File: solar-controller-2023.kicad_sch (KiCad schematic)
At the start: 0 parts

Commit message: add copyright notices
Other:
- note added: "Copyright (C) 2023"
- note added: "Jonathan Bagg"
- note added: "SOLAR CONTROLLER 2023"
- note added: "See https://creativecommons.org/licenses/by-nc-sa/4.0/"
- note added: "v1"

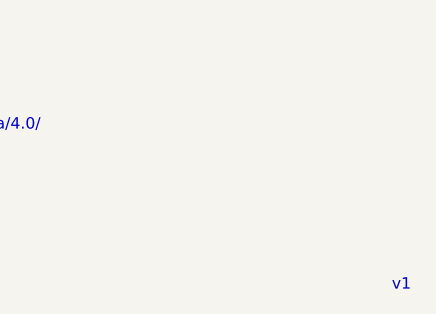
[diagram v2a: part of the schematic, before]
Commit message: AC couple LMT01 signal conditioning and add gain
The difference circuit U3A was DC coupled and so could not
have gain.  Unit gain was only good for sensors up to 15m of
cat-5.
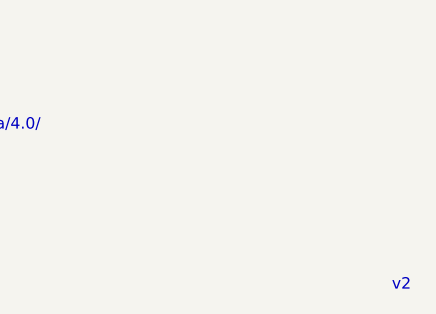
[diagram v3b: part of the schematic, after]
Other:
- note added: "v2"
- note removed: "v1"
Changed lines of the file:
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@@
     )
   )
-  (text "v1" (at 269.24 194.31 0)
+  (text "v2" (at 269.24 194.31 0)
     (effects (font (size 1.27 1.27)) (justify left bottom))
   )
@@
       (reference "#PWR018") (unit 1) (value "GND") (footprint "")
     )
-    (path "/493e9052-9256-45d2-b217-1231bb5dbb20/67602620-6a50-4ac8-bf48-765ca6ca3713"
-      (reference "#PWR019") (unit 1) (value "GND") (footprint "")
-    )
     (path "/493e9052-9256-45d2-b217-1231bb5dbb20/585baf59-dc3a-4d28-882c-d5894ff76c9c"
       (reference "#PWR020") (unit 1) (value "+3V3") (footprint "")
@@
     )
     (path "/493e9052-9256-45d2-b217-1231bb5dbb20/d3ec0c86-c83a-41fb-ba8d-d0db438240cb"
-      (reference "C20") (unit 1) (value "100nF") (footprint "Capacitor_SMD:C_0603_1608Metric_Pad1.08x0.95mm_HandSolder")
+      (reference "C20") (unit 1) (value "680pF") (footprint "Capacitor_SMD:C_0603_1608Metric_Pad1.08x0.95mm_HandSolder")
     )
     (path "/f0385cfa-6958-422f-a694-373ebd16af7a/e37d8436-904b-488c-a95d-9b93d5cb27a7"
@@
       (reference "C38") (unit 1) (value "100nF") (footprint "Capacitor_SMD:C_0603_1608Metric_Pad1.08x0.95mm_HandSolder")
     )
+    (path "/493e9052-9256-45d2-b217-1231bb5dbb20/323ed20a-1d8e-4e2b-96ae-40f84ff376ca"
+      (reference "C39") (unit 1) (value "680pF") (footprint "Capacitor_SMD:C_0603_1608Metric_Pad1.08x0.95mm_HandSolder")
+    )
     (path "/1de4833b-6322-4b99-b5c8-ec67a2e43a06/e530f387-2ae9-42c8-bfd3-533602f3058a"
       (reference "D1") (unit 1) (value "LED") (footprint "Diode_SMD:D_0603_1608Metric_Pad1.05x0.95mm_HandSolder")
@@
       (reference "OUT_7") (unit 1) (value "282837-2") (footprint "project_footprints:282837-2_TYC")
     )
-    (path "/493e9052-9256-45d2-b217-1231bb5dbb20/06b8b026-7bf7-4a1a-a49e-019d3279346a"
-      (reference "Q1") (unit 1) (value "MMBT3906") (footprint "Package_TO_SOT_SMD:SOT-23")
-    )
     (path "/1de4833b-6322-4b99-b5c8-ec67a2e43a06/fd382fec-b21c-4e2d-9067-fa342e870f53"
       (reference "Q2") (unit 1) (value "DTC113Z") (footprint "Package_TO_SOT_SMD:SOT-23")
@@
     )
     (path "/493e9052-9256-45d2-b217-1231bb5dbb20/739a4b9d-9201-4e8c-9e42-b05c1a6fe7a9"
-      (reference "R21") (unit 1) (value "10K") (footprint "Resistor_SMD:R_0603_1608Metric_Pad0.98x0.95mm_HandSolder")
+      (reference "R21") (unit 1) (value "47K") (footprint "Resistor_SMD:R_0603_1608Metric_Pad0.98x0.95mm_HandSolder")
     )
     (path "/493e9052-9256-45d2-b217-1231bb5dbb20/2d952368-7239-4ef5-94e5-398009d53175"
-      (reference "R22") (unit 1) (value "10K") (footprint "Resistor_SMD:R_0603_1608Metric_Pad0.98x0.95mm_HandSolder")
+      (reference "R22") (unit 1) (value "47K") (footprint "Resistor_SMD:R_0603_1608Metric_Pad0.98x0.95mm_HandSolder")
     )
     (path "/493e9052-9256-45d2-b217-1231bb5dbb20/33801c07-f556-4dc7-9f9a-0b87a72c451c"
@@
     )
     (path "/493e9052-9256-45d2-b217-1231bb5dbb20/44174650-586a-4a2a-a370-8a8c422dd70c"
-      (reference "R24") (unit 1) (value "4K7") (footprint "Resistor_SMD:R_0603_1608Metric_Pad0.98x0.95mm_HandSolder")
+      (reference "R24") (unit 1) (value "1K") (footprint "Resistor_SMD:R_0603_1608Metric_Pad0.98x0.95mm_HandSolder")
     )
     (path "/493e9052-9256-45d2-b217-1231bb5dbb20/e6380c5d-47ae-4b48-9a69-e22fd1678d80"
@@
     )
     (path "/493e9052-9256-45d2-b217-1231bb5dbb20/55913f4c-3b65-4087-85a0-b8f09529be23"
-      (reference "R26") (unit 1) (value "10K") (footprint "Resistor_SMD:R_0603_1608Metric_Pad0.98x0.95mm_HandSolder")
+      (reference "R26") (unit 1) (value "1K") (footprint "Resistor_SMD:R_0603_1608Metric_Pad0.98x0.95mm_HandSolder")
     )
     (path "/f0385cfa-6958-422f-a694-373ebd16af7a/10848a90-cebd-4104-8b34-36567881cc3a"
@@
       (reference "R44") (unit 1) (value "0") (footprint "Resistor_SMD:R_0603_1608Metric_Pad0.98x0.95mm_HandSolder")
     )
+    (path "/493e9052-9256-45d2-b217-1231bb5dbb20/34f6ce72-f94d-431f-92ae-8c1459853424"
+      (reference "R45") (unit 1) (value "4K7") (footprint "Resistor_SMD:R_0603_1608Metric_Pad0.98x0.95mm_HandSolder")
+    )
     (path "/1de4833b-6322-4b99-b5c8-ec67a2e43a06/f8d0a2b6-69b6-461b-9d3c-3ea118392741"

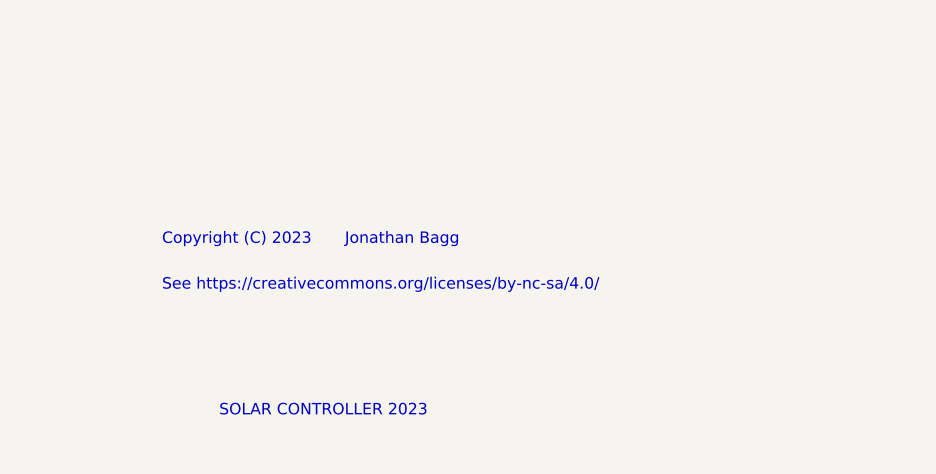
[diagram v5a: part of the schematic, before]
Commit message: add github link to title block and print schematic pdf
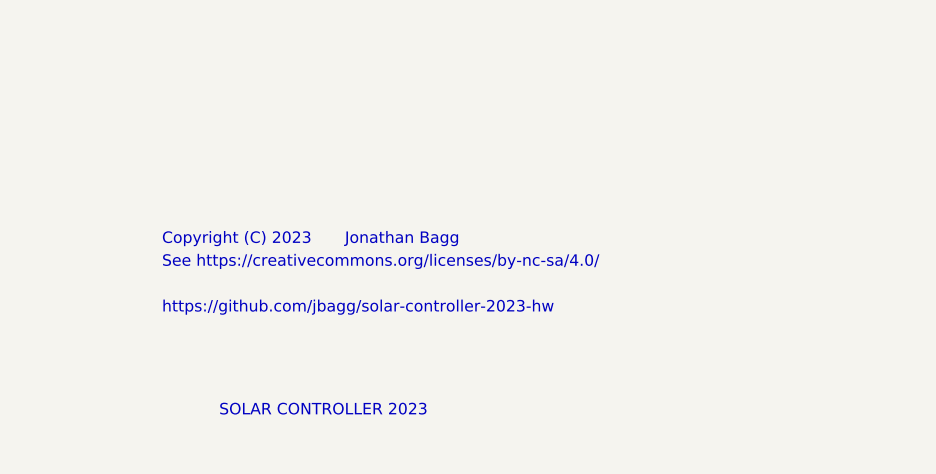
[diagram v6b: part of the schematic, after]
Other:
- note added: "https://github.com/jbagg/solar-controller-2023-hw"
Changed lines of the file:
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@@
   )
   (text "See https://creativecommons.org/licenses/by-nc-sa/4.0/"
-    (at 181.61 176.53 0)
+    (at 181.61 173.99 0)
     (effects (font (size 1.27 1.27)) (justify left bottom))
   )
+  (text "https://github.com/jbagg/solar-controller-2023-hw" (at 181.61 179.07 0)
+    (effects (font (size 1.27 1.27)) (justify left bottom))
+  )
